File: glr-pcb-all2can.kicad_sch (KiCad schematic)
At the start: 30 parts, among them IC2 ZMR330FTA, IC3 AP64060WU-7, IC4 STM32C092KCT6, J1 DA15_Pins_MountingHoles, J2 Conn_02x03_Top_Bottom, J3 Conn_01x04, J4 Conn_01x02, J5 Conn_01x02

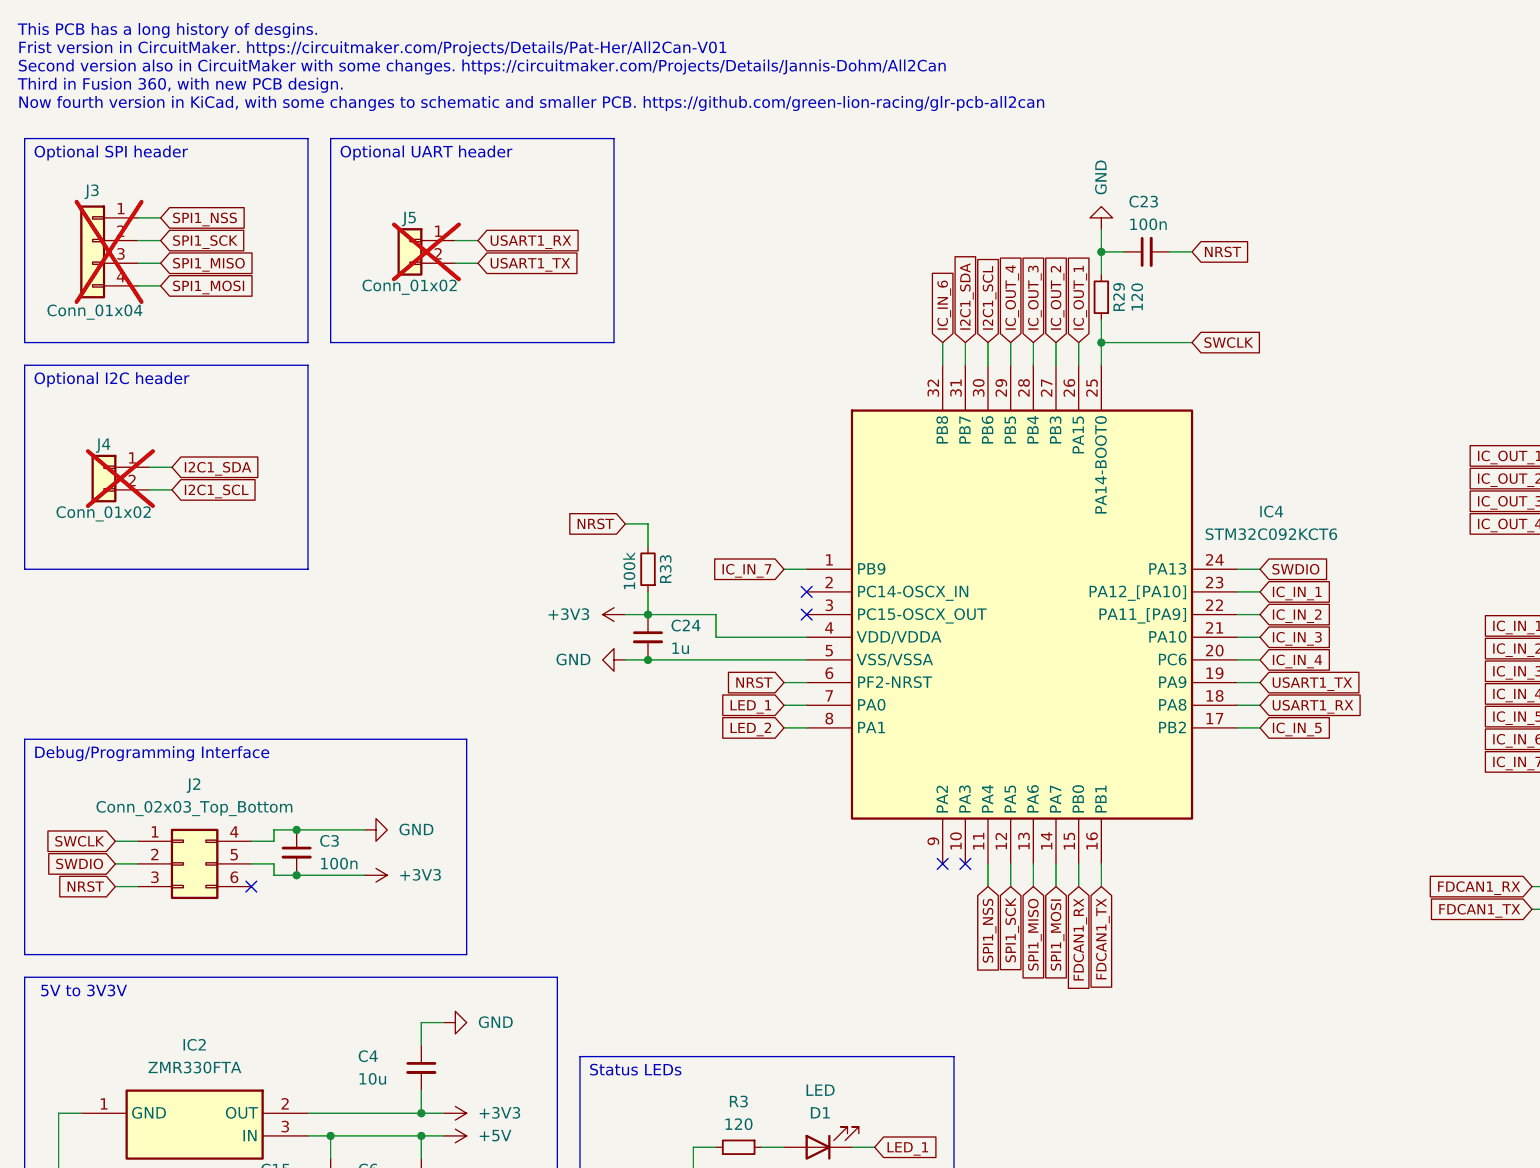
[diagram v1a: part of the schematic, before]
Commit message: change swd header
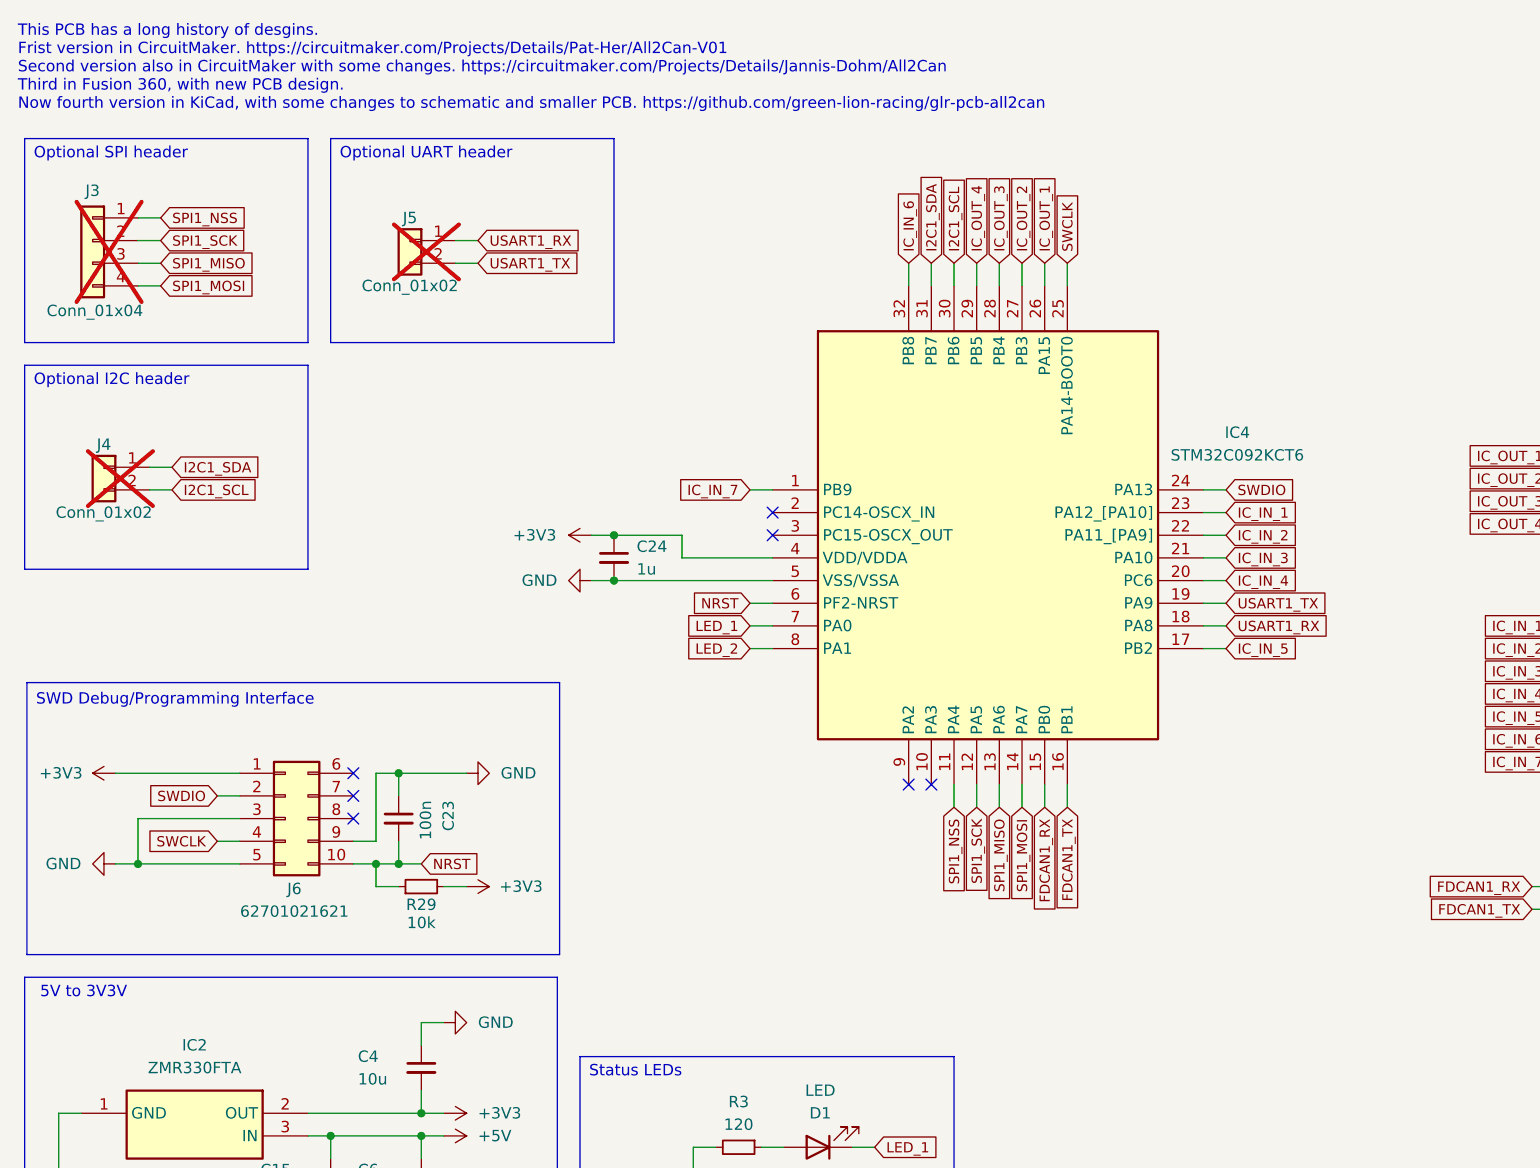
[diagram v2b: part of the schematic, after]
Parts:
- removed C3: 100n, Capacitor_SMD:C_0603_1608Metric, symbol Device:C_Small
- removed J2: Conn_02x03_Top_Bottom, Connector_PinHeader_2.54mm:PinHeader_2x03_P2.54mm_Vertical, symbol Connector_Generic:Conn_02x03_Top_Bottom
- removed R33: 100k, Resistor_SMD:R_0603_1608Metric, symbol Device:R_Small
- added J6: 62701021621, SamacSys_Parts:62701021621, symbol Connector_Generic:Conn_02x05_Top_Bottom
- R29: value 120 -> 10k
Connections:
- net +3V3: now also R29.2, J6.1 (Pin_1)
- net GND: now also J6.3 (Pin_3), J6.5 (Pin_5), J6.9 (Pin_9); no longer R29.2
- net NRST: now also R29.1, J6.10 (Pin_10)
- net SWCLK: now also J6.4 (Pin_4); no longer R29.1
- net SWDIO: now also J6.2 (Pin_2)
- no-connect marks 5 -> 7
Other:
- note added: "SWD Debug/Programming Interface"
- note removed: "Debug/Programming Interface"
- moved on the sheet: C23, C24, IC4, R29

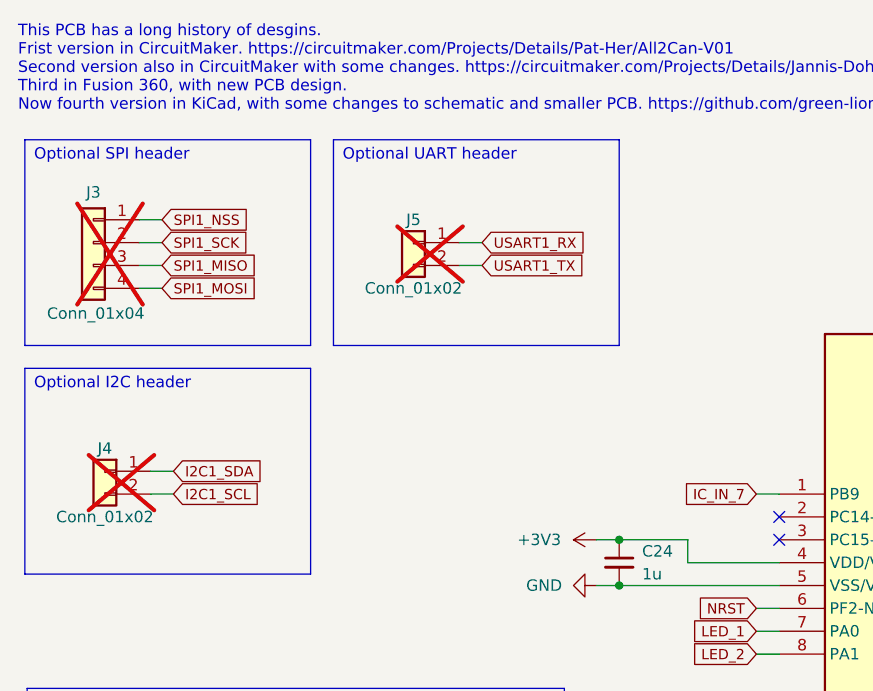
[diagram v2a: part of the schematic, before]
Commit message: reorder more
move pullup i2c in schematic
make power passing routes thicker
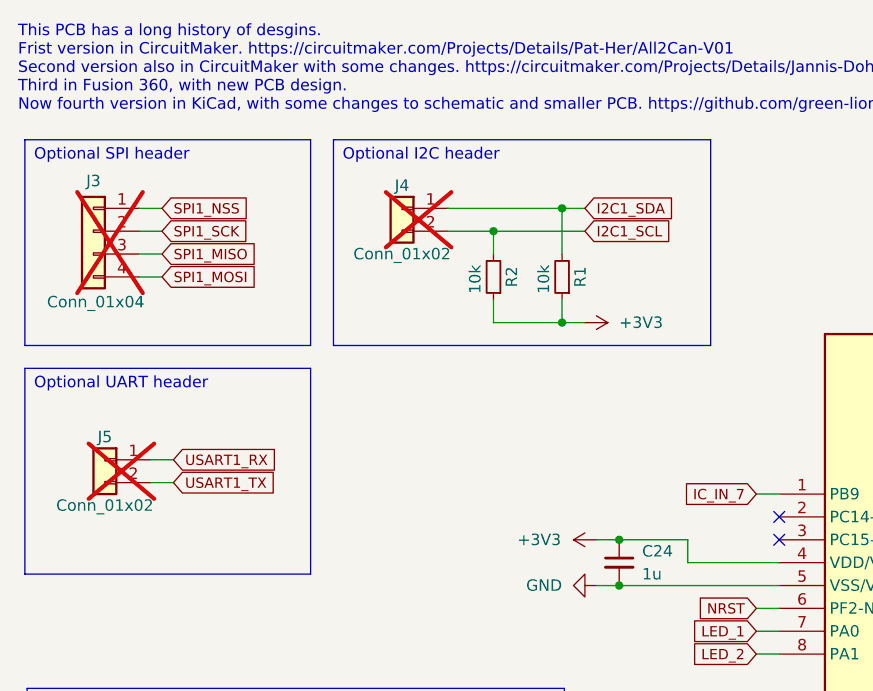
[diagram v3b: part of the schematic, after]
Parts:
- added R1, R2: 10k, Resistor_SMD:R_0603_1608Metric, symbol Device:R_Small
- J3: footprint Connector_PinHeader_2.54mm:PinHeader_1x04_P2.54mm_Vertical -> Connector_PinHeader_1.27mm:PinHeader_1x04_P1.27mm_Vertical
- J4, J5: footprint Connector_PinHeader_2.54mm:PinHeader_1x02_P2.54mm_Vertical -> Connector_PinHeader_1.27mm:PinHeader_1x02_P1.27mm_Vertical
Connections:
- net +3V3: now also R1.1, R2.1
- net I2C1_SCL: now also R2.2
- net I2C1_SDA: now also R1.2
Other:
- moved on the sheet: J3, J4, J5

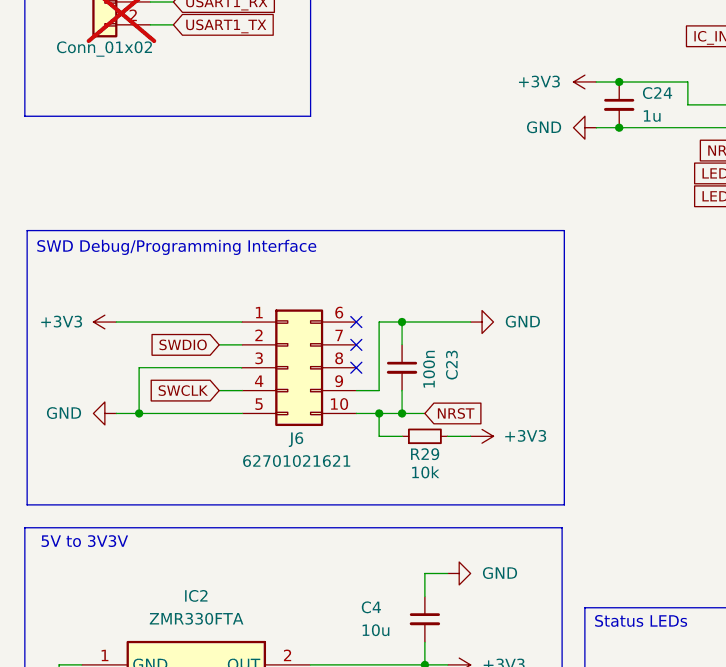
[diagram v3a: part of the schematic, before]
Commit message: add missing pull down resistor for swd
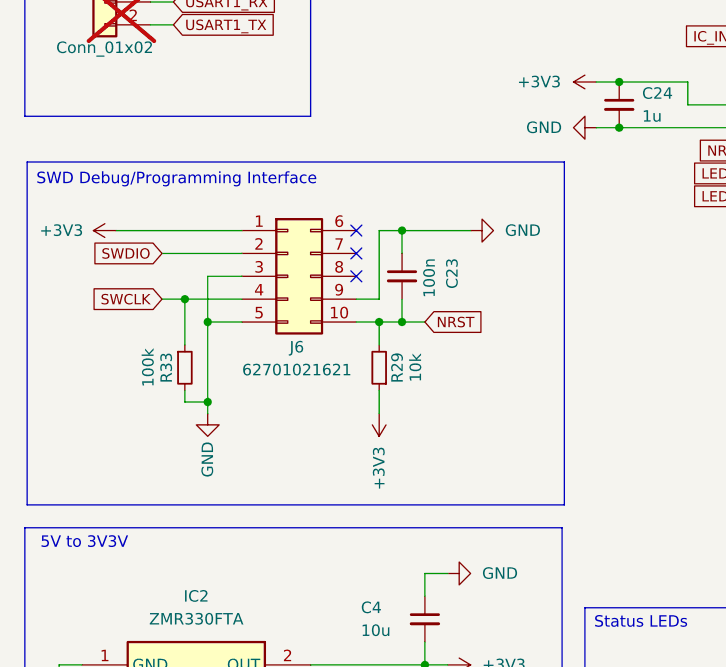
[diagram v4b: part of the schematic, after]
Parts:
- added R33: 100k, Resistor_SMD:R_0603_1608Metric, symbol Device:R_Small
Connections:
- net +3V3: now also R29.1; no longer R29.2
- net GND: now also R33.2
- net NRST: now also R29.2; no longer R29.1
- net SWCLK: now also R33.1
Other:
- moved on the sheet: C23, J6, R29

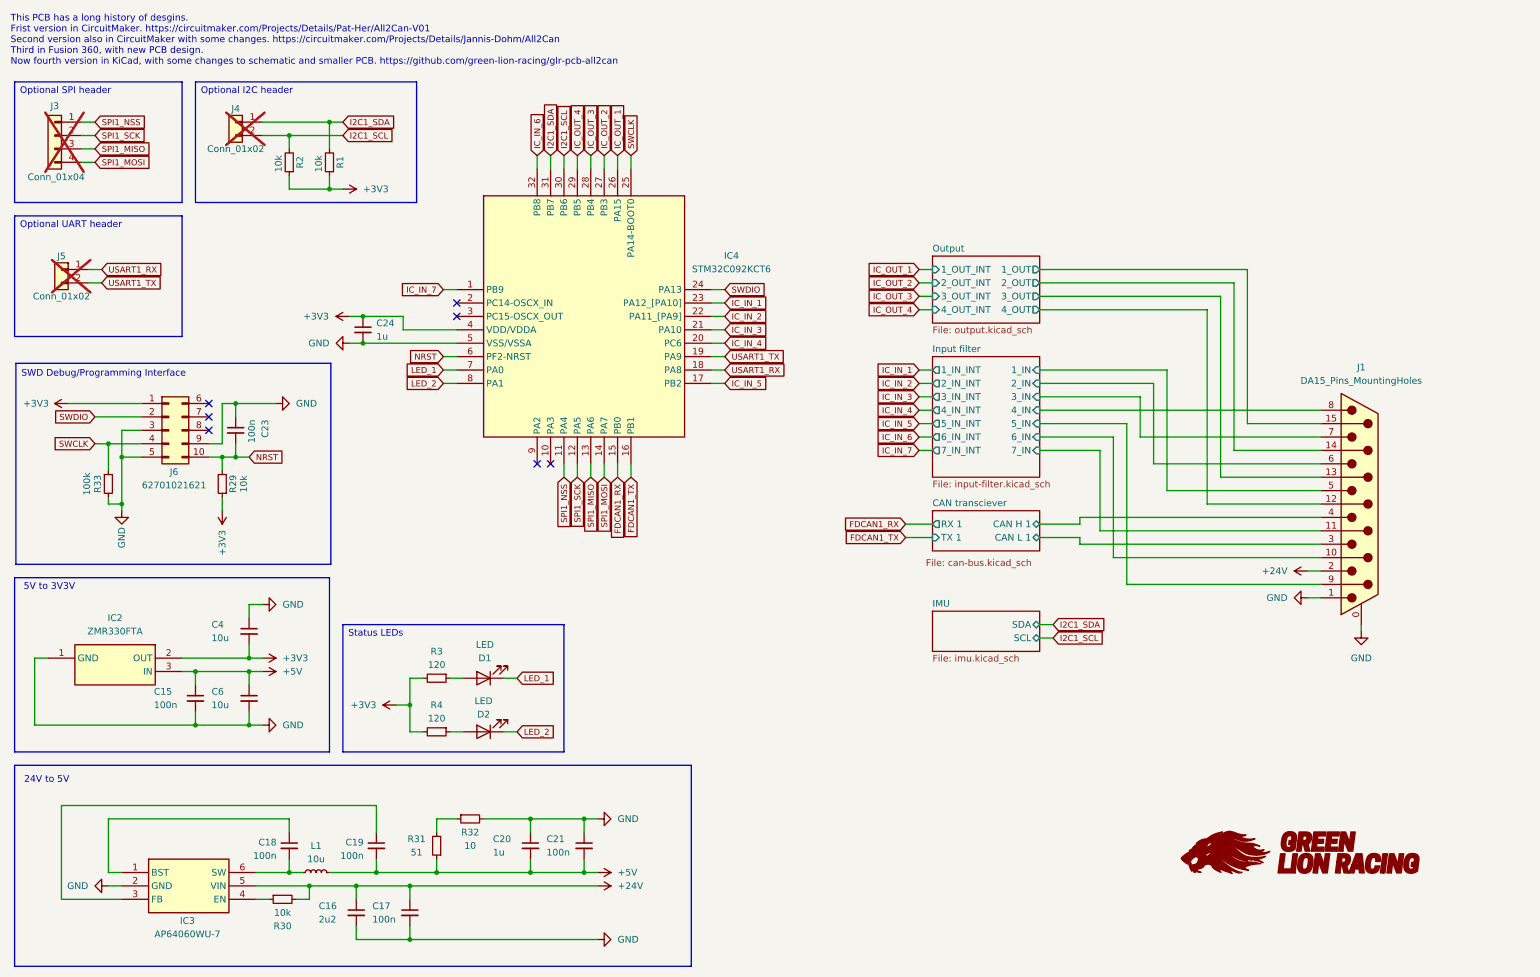
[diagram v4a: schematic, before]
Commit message: massive overhaul of pcb
* replace sub-d with 4x m12a 4pin circular connector
* fit board to bopla bolink case
* restructure entire board
* add second main voltage converter for powering input devices
* reduce inputs to 5
* remove 6 axis imu
* remove outputs
* remove mounting holes
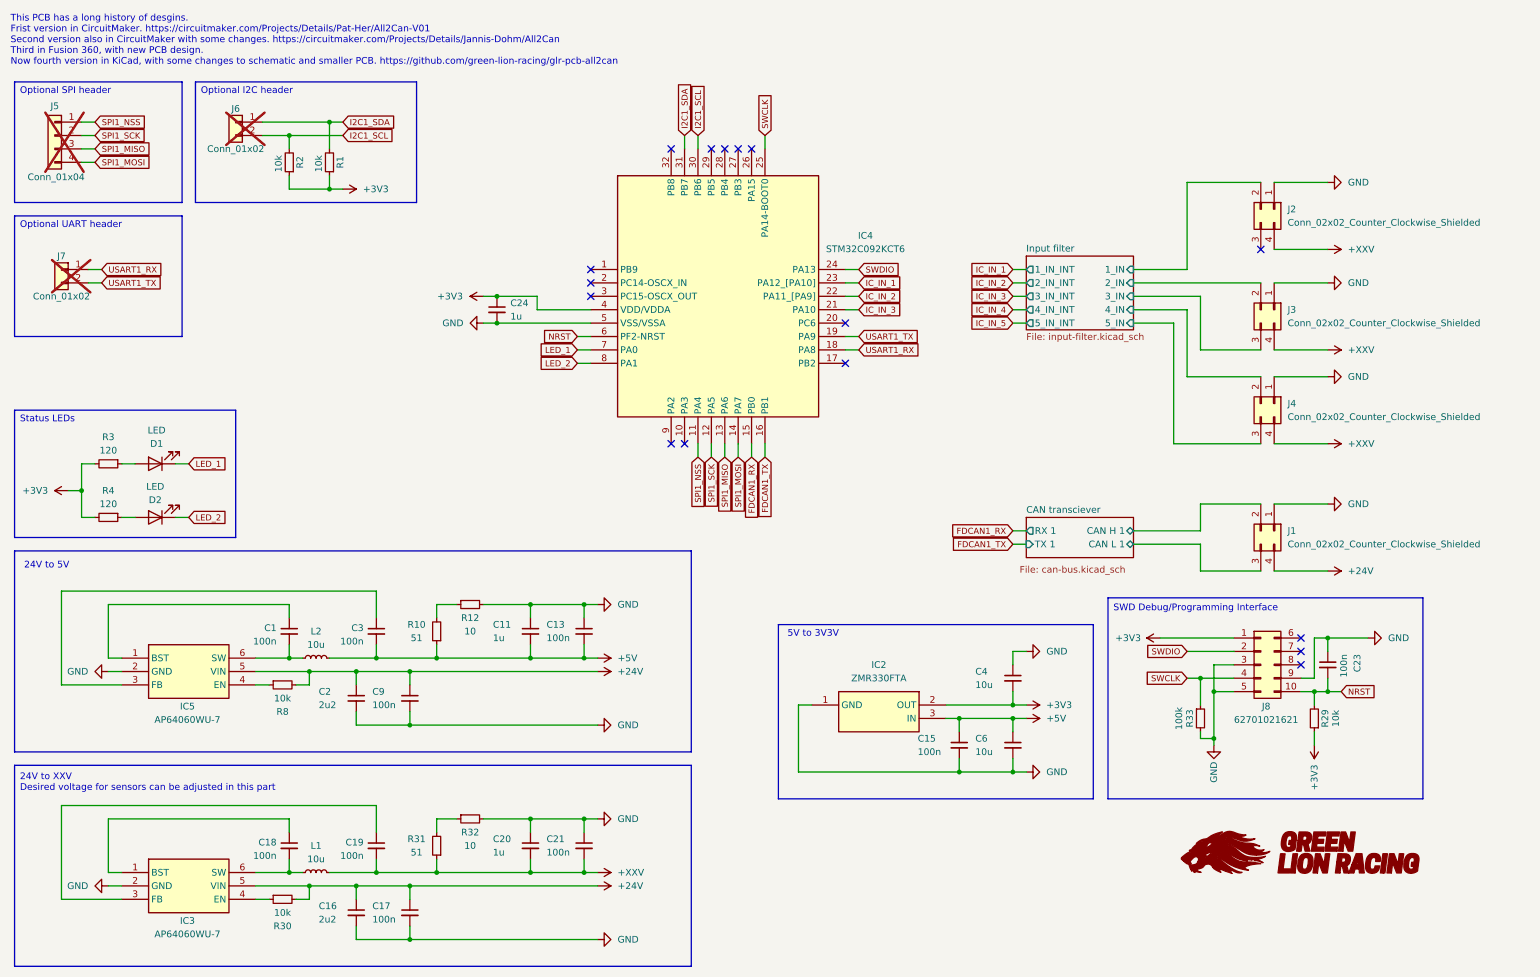
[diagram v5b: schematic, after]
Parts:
- removed J1: DA15_Pins_MountingHoles, Connector_Dsub:DSUB-15-HD_Pins_Horizontal_P2.29x1.90mm_EdgePinOffset3.03mm_Housed_MountingHolesOffset4.94mm, symbol Connector:DA15_Pins_MountingHoles
- added C1, C13, C3, C9: 100n, Capacitor_SMD:C_0603_1608Metric, symbol Device:C_Small
- added C11: 1u, Capacitor_SMD:C_0603_1608Metric, symbol Device:C_Small
- added C2: 2u2, Capacitor_SMD:C_0603_1608Metric, symbol Device:C_Small
- added IC5: AP64060WU-7, SamacSys_Parts:SOT95P280X100-6N, symbol SamacSys_Parts:AP64060WU-7
- added J1, J2, J3, J4: Conn_02x02_Counter_Clockwise_Shielded, GLR_KiCad_Library:M12A-04P, symbol Connector_Generic:Conn_02x02_Counter_Clockwise
- added L2: 10u, Inductor_SMD:L_1008_2520Metric, symbol Device:L_Small
- added R10: 51, Resistor_SMD:R_0603_1608Metric, symbol Device:R_Small
- added R12: 10, Resistor_SMD:R_0603_1608Metric, symbol Device:R_Small
- added R8: 10k, Resistor_SMD:R_0603_1608Metric, symbol Device:R_Small
- renumbered J3 to J5, J4 to J6, J5 to J7, J6 to J8
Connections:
- net +24V: now also C2.1, C9.1, IC5.5 (VIN), J1.4 (Pin_4), R8.2
- net +5V: now also C11.2, C13.2, C3.2, L2.2, R10.1; no longer C19.2, C20.2, C21.2, L1.2, R31.1
- net CAN transciever/CAN H 1: now also J1.2 (Pin_2)
- net CAN transciever/CAN L 1: now also J1.3 (Pin_3)
- net GND: now also C11.1, C13.1, C2.2, C9.2, IC5.2 (GND), J1.1 (Pin_1), J2.1 (Pin_1), J3.1 (Pin_1), J4.1 (Pin_1), R12.2
- net IC_IN_4: no longer IC4.20 (PC6)
- net IC_IN_5: no longer IC4.17 (PB2)
- net Input filter/1_IN: now also J2.2 (Pin_2)
- net Input filter/2_IN: now also J3.2 (Pin_2)
- net Input filter/3_IN: now also J3.3 (Pin_3)
- net Input filter/4_IN: now also J4.2 (Pin_2)
- net Input filter/5_IN: now also J4.3 (Pin_3)
- net IC_IN_6: no longer names the net of IC4.32 (PB8)
- net IC_IN_7: no longer names the net of IC4.1 (PB9)
- net IC_OUT_1: no longer names the net of IC4.26 (PA15)
- net IC_OUT_2: no longer names the net of IC4.27 (PB3)
- net IC_OUT_3: no longer names the net of IC4.28 (PB4)
- net IC_OUT_4: no longer names the net of IC4.29 (PB5)
- new net: C1.2, IC5.6 (SW), L2.1
- new net: C1.1, IC5.1 (BST)
- new net: C3.1, IC5.3 (FB)
- new net: IC5.4 (EN), R8.1
- new net: R10.2, R12.1
- new net +XXV: C19.2, C20.2, C21.2, J2.4 (Pin_4), J3.4 (Pin_4), J4.4 (Pin_4), L1.2, R31.1
- no-connect marks 7 -> 16
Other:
- removed sheet IMU
- removed sheet Output
- sheet Input filter ports: added none; removed 6_IN, 6_IN_INT, 7_IN, 7_IN_INT
- note added: "24V to XXV Desired voltage for sensors can be adjusted in this part"
- moved on the sheet: C15, C23, C24, C4, C6, D1, D2, IC2, IC4, J8, R29, R3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
